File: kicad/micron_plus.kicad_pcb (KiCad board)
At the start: 2 copper layers, 163.8 x 123.2 mm, 78 parts, among them J1 Conn_02x17_Odd_Even, J2 Screw_Terminal_01x02, Q1 2N2905A, Q2 2N2905A, Q3 2N3904, Q4 2N3904, T1 Transformer_1P_2S, U1 MC68A21, U10 74LS00, U11 7406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

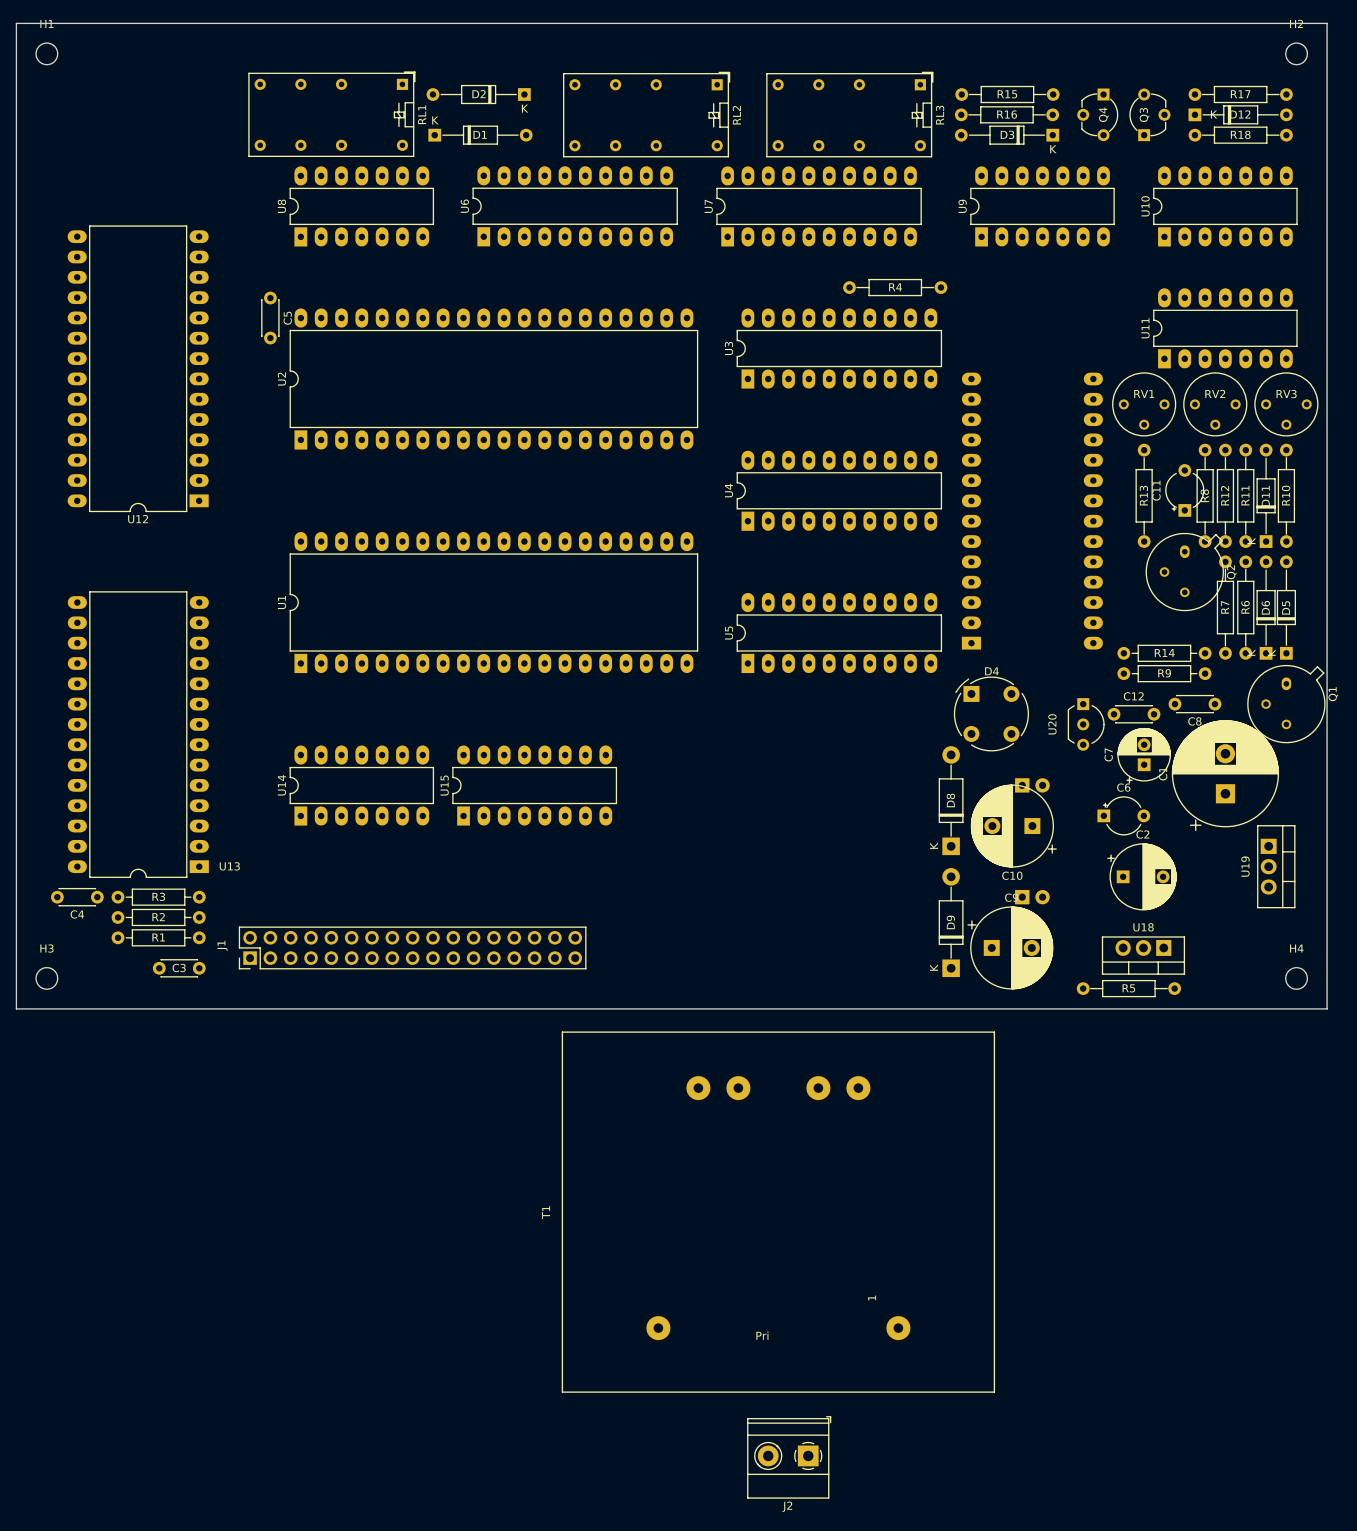
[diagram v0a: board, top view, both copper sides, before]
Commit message: KiCAD: PCB now routed
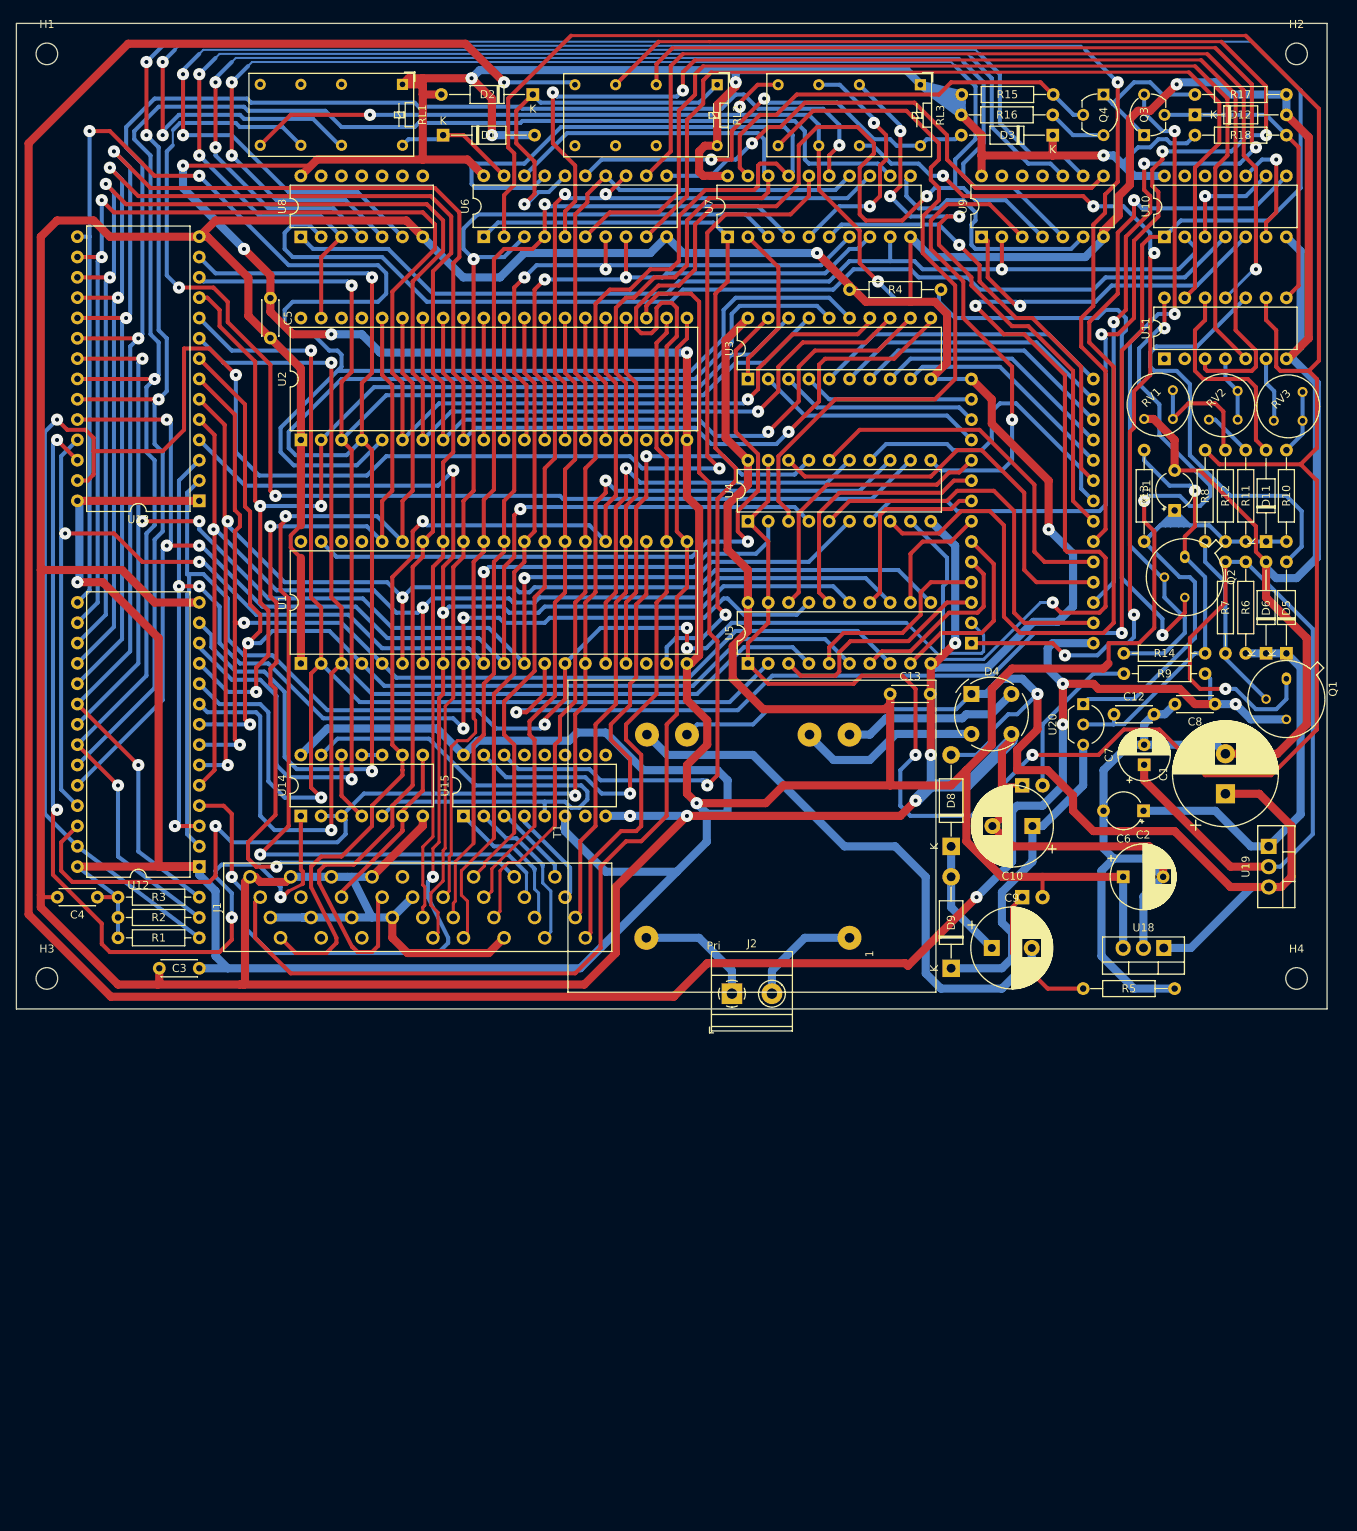
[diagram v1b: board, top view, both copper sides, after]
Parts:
- added C13: 100n, Capacitor_THT:C_Disc_D4.3mm_W1.9mm_P5.00mm, F.Cu at (149.9, 105.4)
- J1: footprint Connector_PinHeader_2.54mm:PinHeader_2x17_P2.54mm_Vertical -> custom_footprints:TransitionHeader_34_P2.54mm_Vertical
- T1: footprint custom_footprints:Transformer_vigortronix_12VA_2xSec -> custom_footprints:Transformer_drake_p0609
- U1, U2: footprint Package_DIP:DIP-40_W15.24mm_LongPads -> Package_DIP:DIP-40_W15.24mm
- U10, U11, U14, U8, U9: footprint Package_DIP:DIP-14_W7.62mm_LongPads -> Package_DIP:DIP-14_W7.62mm
- U12, U13: footprint Package_DIP:DIP-28_W15.24mm_LongPads -> Package_DIP:DIP-28_W15.24mm
- U15: footprint Package_DIP:DIP-16_W7.62mm_LongPads -> Package_DIP:DIP-16_W7.62mm
- U17: footprint Package_DIP:DIP-28_W15.24mm_Socket_LongPads -> Package_DIP:DIP-28_W15.24mm_Socket
- U3, U4, U5, U6, U7: footprint Package_DIP:DIP-20_W7.62mm_LongPads -> Package_DIP:DIP-20_W7.62mm
- moved J2 58.6 mm to (130.1, 142.9), turned to 0 degrees
- moved T1 49.2 mm to (144.8, 135.9)
- moved U13 45.7 mm to (63.5, 81.3)
- moved U12 45.7 mm to (63.5, 127.0)
- moved J1 10.2 mm to (69.8, 128.3)
- moved R14 10.2 mm to (189.2, 100.3), turned to 180 degrees
- moved R9 10.2 mm to (189.2, 102.9), turned to 180 degrees
- moved C6 5.00 mm to (181.5, 120.0), turned to 180 degrees
- moved RV1 2.06 mm to (185.2, 67.4), turned to 135 degrees
- moved RV2 1.71 mm to (193.3, 67.5), turned to 135 degrees
- moved RV3 1.64 mm to (201.4, 67.7), turned to 135 degrees
- moved C11 1.27 mm to (185.4, 82.5)
- moved D1 1.05 mm to (94.0, 35.6)
- moved D2 1.05 mm to (105.2, 30.5)
- moved Q1 0.64 mm to (199.4, 103.5)
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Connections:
- net Net-(U13-Pad26) renamed /Buffer RAM/nAddr13
- RV1 pad 1: GND -> Net-(R12-Pad1)
- RV1 pad 3: Net-(R12-Pad1) -> GND
- RV2 pad 2: Net-(R11-Pad1) -> Net-(RV2-Pad1)
- RV3 pad 1: Net-(RV3-Pad1) -> Net-(R10-Pad1)
- RV3 pad 3: Net-(R10-Pad1) -> Net-(RV3-Pad3)
- T1 pad 1: Net-(J2-Pad1) -> Net-(J2-Pad2)
- T1 pad 2: Net-(J2-Pad2) -> Net-(J2-Pad1)
- T1 pad 3: Net-(C9-Pad2) -> Net-(D4-Pad4)
- T1 pad 4: /Power Supply/10VDC -> Net-(D4-Pad2)
- T1 pad 5: Net-(D4-Pad4) -> /Power Supply/10VDC
- T1 pad 6: Net-(D4-Pad2) -> Net-(C9-Pad2)
- U11 pad 6: Net-(RV3-Pad1) -> Net-(RV3-Pad3)
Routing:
- net GND: track 0.00 -> 974.4 mm, vias 0 -> 8
- net VCC: track 0.00 -> 894.6 mm, vias 0 -> 12
- net /1MHz Bus and PIA Interface/Addr11: track 0.00 -> 425.1 mm, vias 0 -> 5
- net /Main Logic and Eprom Socket/EpromVCC: track 0.00 -> 378.0 mm, vias 0 -> 5
- net /Control Latches/nVCCEnable: track 0.00 -> 361.7 mm, vias 0 -> 2
- net /1MHz Bus and PIA Interface/Addr12: track 0.00 -> 287.3 mm, vias 0 -> 6
- net /1MHz Bus and PIA Interface/LatchB: track 0.00 -> 252.5 mm, vias 0 -> 3
- net /Control Latches/nRAMWE: track 0.00 -> 237.7 mm, vias 0 -> 3
- net /1MHz Bus and PIA Interface/Data3: track 0.00 -> 233.2 mm, vias 0 -> 2
- net /Control Latches/nRAMOE: track 0.00 -> 223.5 mm, vias 0 -> 2
- net /1MHz Bus and PIA Interface/Data7: track 0.00 -> 220.8 mm, vias 0 -> 3
- net /Main Logic and Eprom Socket/Eprom23VPP: track 0.00 -> 217.5 mm, vias 0 -> 3
- net /Control Latches/nRAMCE: track 0.00 -> 215.4 mm, vias 0 -> 3
- net /1MHz Bus and PIA Interface/Data6: track 0.00 -> 213.6 mm, vias 0 -> 3
- net /1MHz Bus and PIA Interface/Data2: track 0.00 -> 209.5 mm, vias 0 -> 2
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
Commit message: KiCAD: Tidying errors/warnings
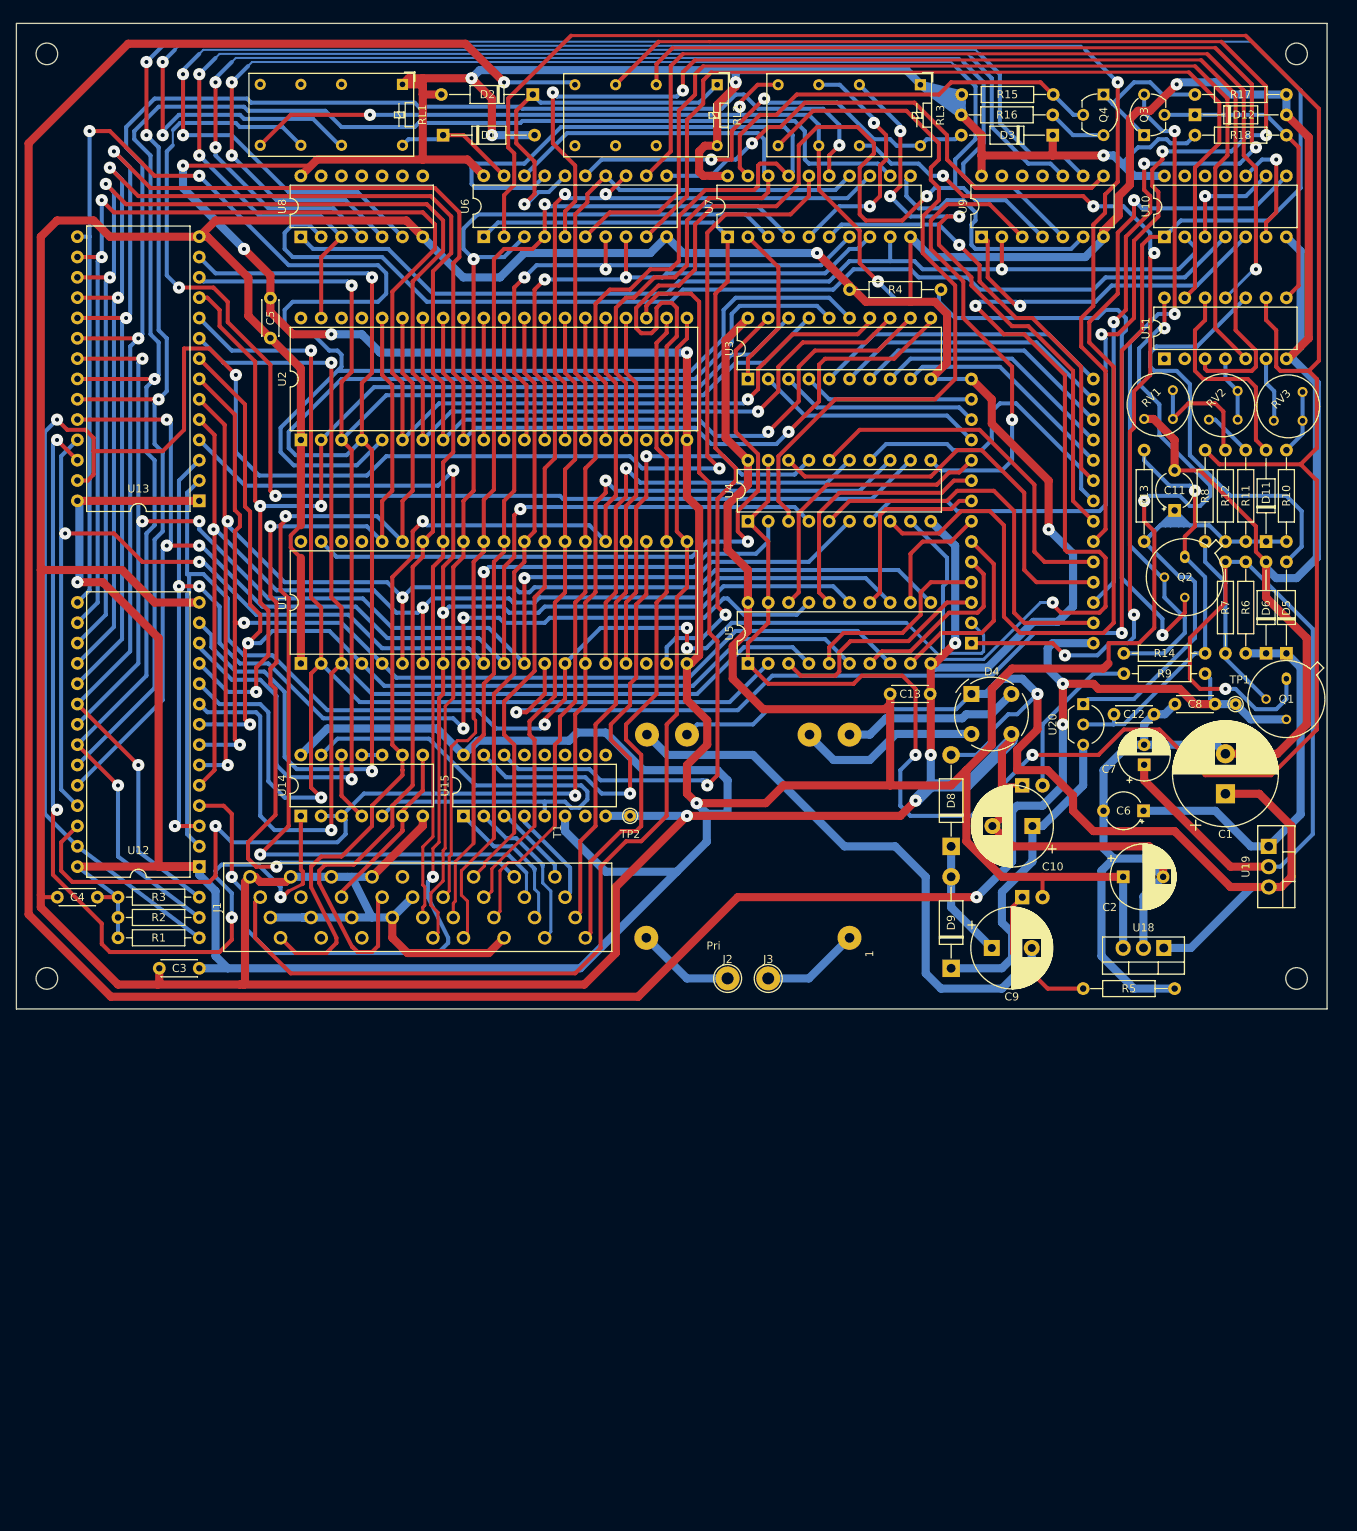
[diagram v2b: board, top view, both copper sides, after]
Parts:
- added J3: Conn_01x01_Female, TestPoint:TestPoint_THTPad_D3.0mm_Drill1.5mm, F.Cu at (134.6, 141.0)
- added TP1: TestPoint, TestPoint:TestPoint_THTPad_D1.5mm_Drill0.7mm, F.Cu at (193.0, 106.7)
- added TP2: TestPoint, TestPoint:TestPoint_THTPad_D1.5mm_Drill0.7mm, F.Cu at (117.3, 120.7)
- J2: value Screw_Terminal_01x02 -> Conn_01x01_Female; footprint TerminalBlock_Phoenix:TerminalBlock_Phoenix_MKDS-1,5-2_1x02_P5.00mm_Horizontal -> TestPoint:TestPoint_THTPad_D3.0mm_Drill1.5mm
- moved J2 1.98 mm to (129.5, 141.0)
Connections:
- T1 pad 1: Net-(J2-Pad2) -> Net-(J3-Pad1)
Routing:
- net Net-(J2-Pad2): track 14.3 -> 0.00 mm
- net Net-(J3-Pad1): track 0.00 -> 12.3 mm
- net Net-(J2-Pad1): track 15.3 -> 12.3 mm
- net /Main Logic and Eprom Socket/EpromVCC: track 378.0 -> 377.8 mm, vias 5 -> 4
- net GND: vias 8 -> 7

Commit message: KiCAD: Adjust courtyards
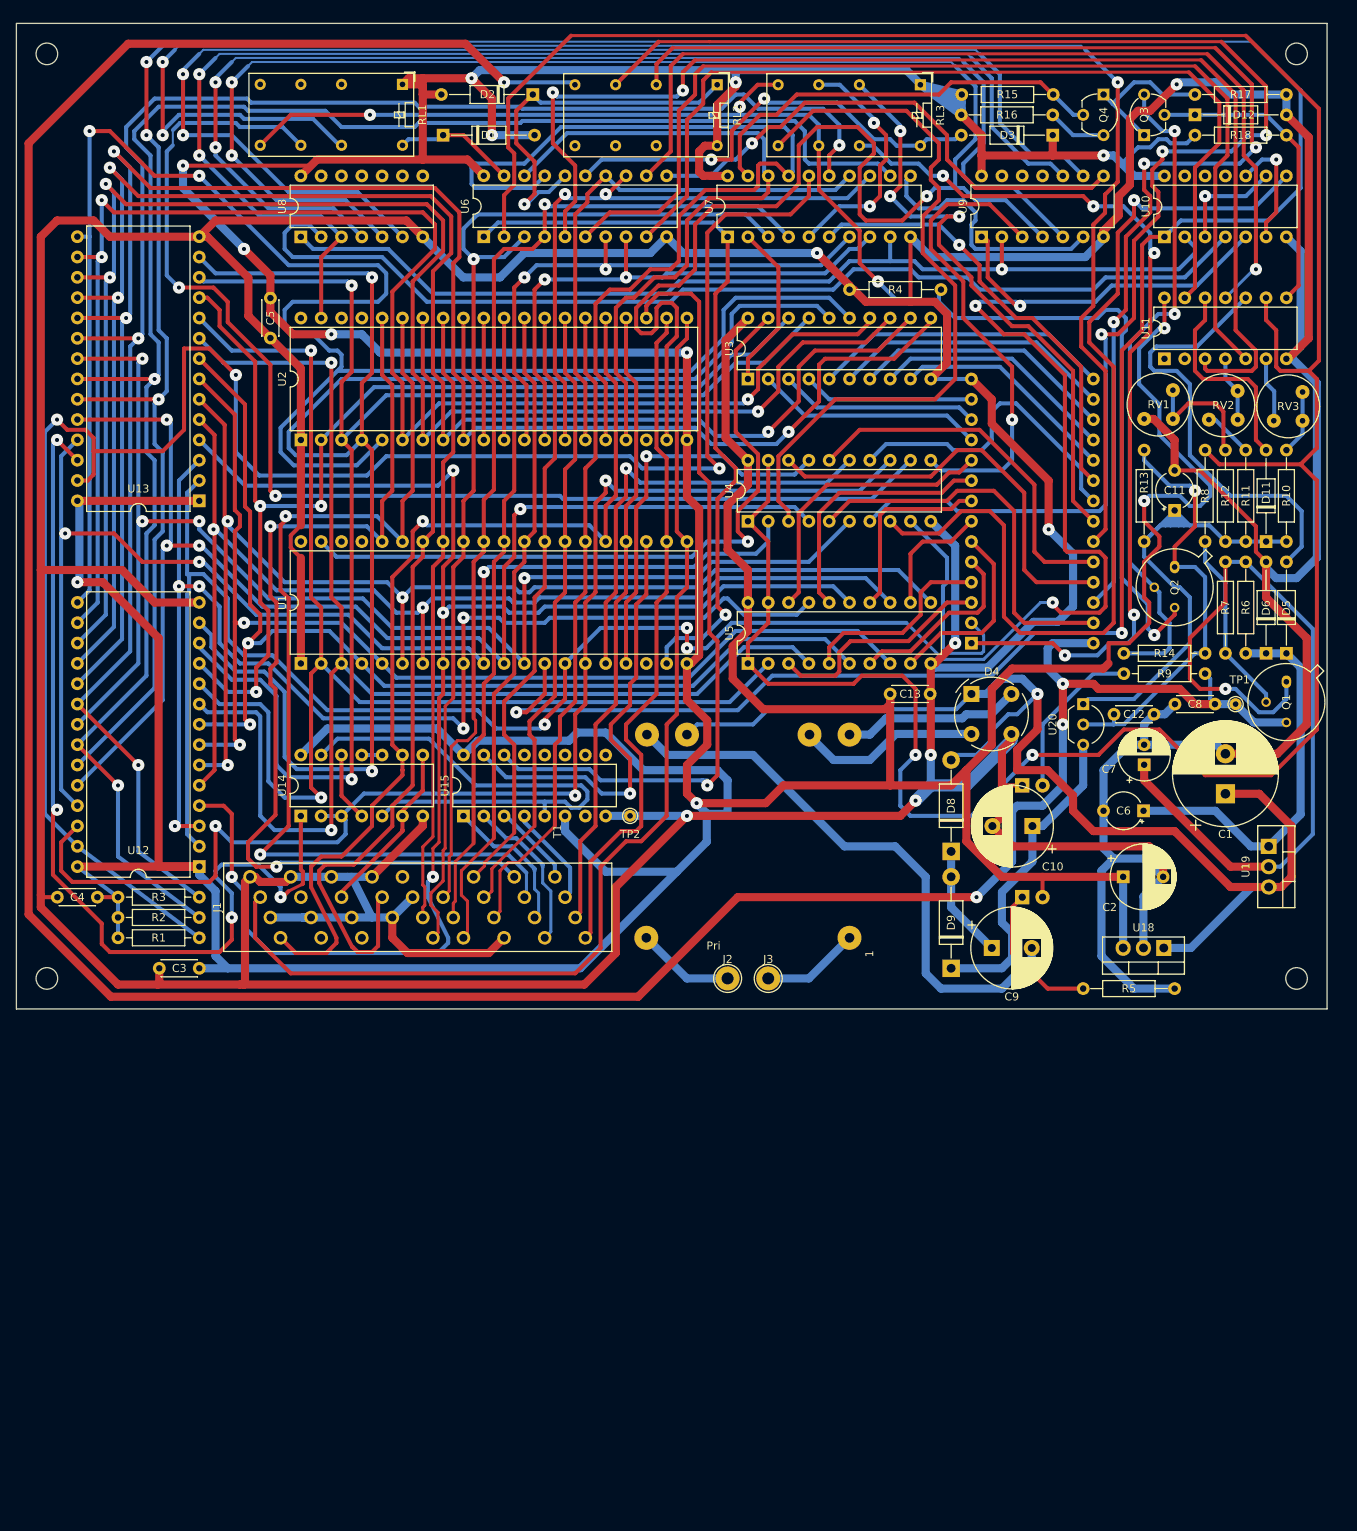
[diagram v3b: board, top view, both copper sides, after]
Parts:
- C11, C6: footprint Capacitor_THT:CP_Radial_Tantal_D4.5mm_P5.00mm -> custom_footprints:CP_Radial_Tantal_D4.5mm_P5.00mm
- Q1, Q2: footprint Package_TO_SOT_THT:TO-39-3 -> custom_footprints:TO-39-3
- RV1, RV2, RV3: footprint Potentiometer_THT:Potentiometer_Bourns_3339P_Vertical -> custom_footprints:Potentiometer_Bourns_3339P_Vertical_HandSoldering
- moved Q2 1.80 mm to (185.4, 89.5)
- moved D8 0.64 mm to (157.5, 125.1)
- moved Q1 0.38 mm to (199.4, 103.9)
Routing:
- net Net-(C12-Pad1): track 51.2 -> 53.8 mm
- net Net-(Q2-Pad2): track 85.0 -> 83.2 mm
- net /Main Logic and Eprom Socket/EpromVPP: track 184.6 -> 182.8 mm
- net Net-(C11-Pad1): track 67.0 -> 66.1 mm
- net Net-(C9-Pad1): track 14.8 -> 14.2 mm
